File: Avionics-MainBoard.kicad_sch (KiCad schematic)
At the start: 4 parts

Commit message: v3 Layout complete
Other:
- sheet Connectors ports: added COIL_EN, HEATER0_ON, HEATER1_ON, HEATER_ENABLE, RW_EN; removed none
- sheet LoRa ports: added LoRa_CSn, LoRa_FLT; removed CSn
- sheet MCU_IO ports: added 3V3_M_RST, 3V3_P_EN, 3V3_P_FLT, COIL_EN, GPS_EN, GPS_FLT, HEATER0_ON, HEATER1_ON, HEATER_ENABLE, LoRa_FLT, Payload_CSn, Payload_EN, Payload_FLT, Payload_IO0, Payload_IO1, Payload_IO2, RW_EN; removed 3V3_RST
- sheet Main Power ports: added 3V3_P_FLT; removed none
- sheet Payload ports: added CLK, MISO, MOSI, Payload_CSn, Payload_EN, Payload_FLT, Payload_IO0, Payload_IO1, Payload_IO2; removed none
- sheet SD ports: added SD_CSn; removed CSn

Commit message: v4.0 Updates
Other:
- removed sheet Payload
- sheet Connectors ports: added RW_MOTOR_ALRM, RW_MOTOR_FLT, RW_POWER_FLT; removed none
- sheet MCU_IO ports: added none; removed Payload_CSn, Payload_EN, Payload_FLT, Payload_IO0, Payload_IO1, Payload_IO2
- note added: "TODO: CLEANUP"
- note added: "Unconnected Cutting RW from Argus 1/2"
- moved on the sheet: H1, H2, H3, H4

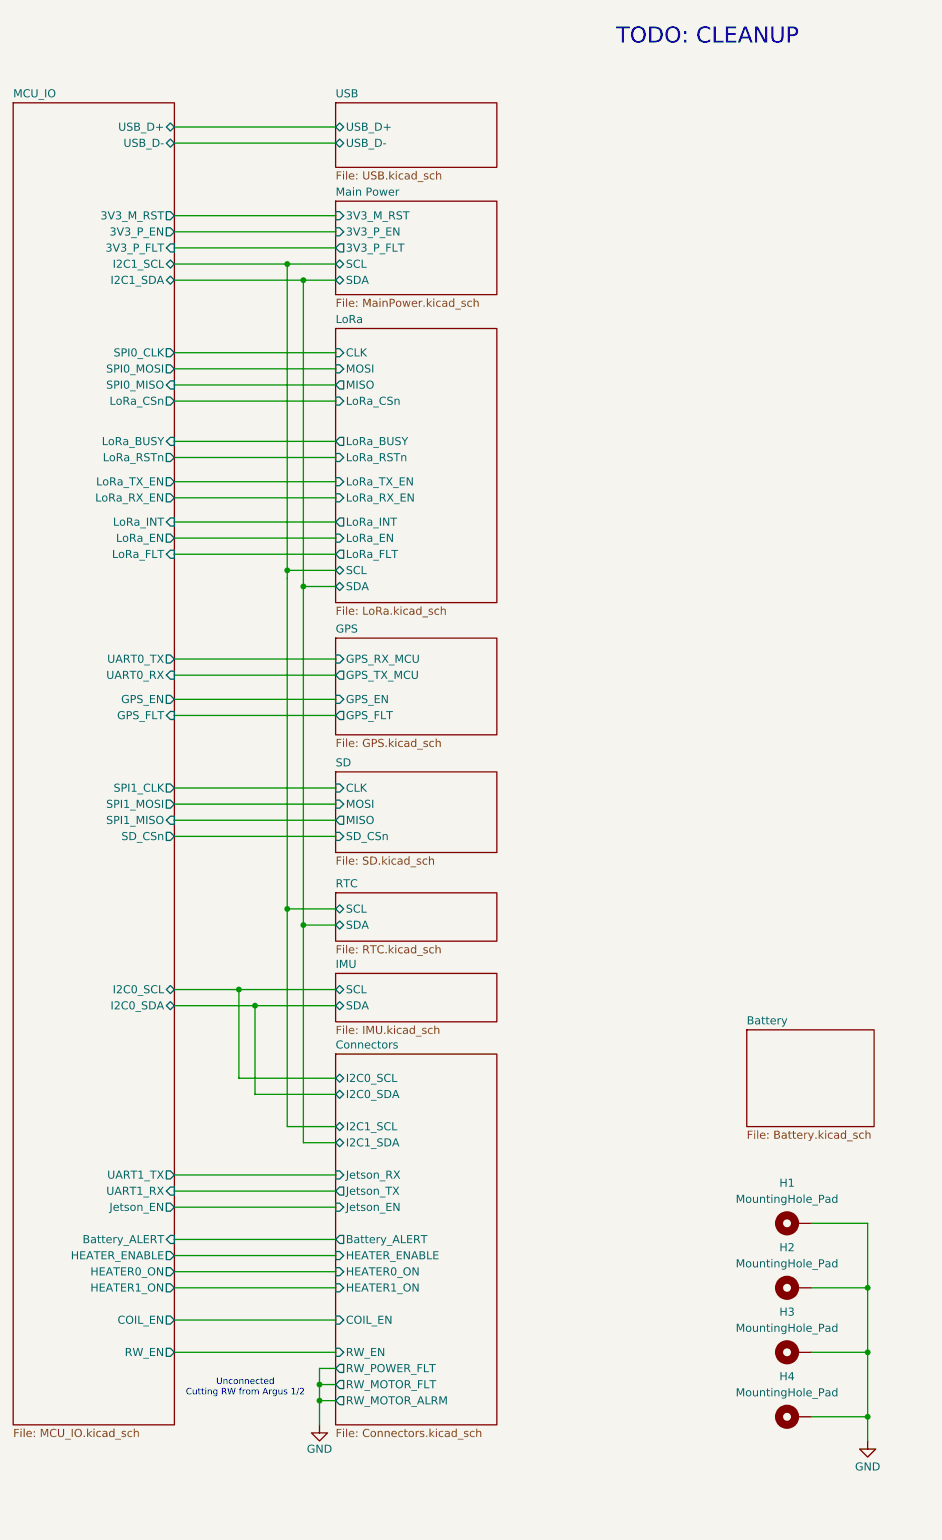
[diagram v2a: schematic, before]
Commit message: Fixed Jetson FPC pinout
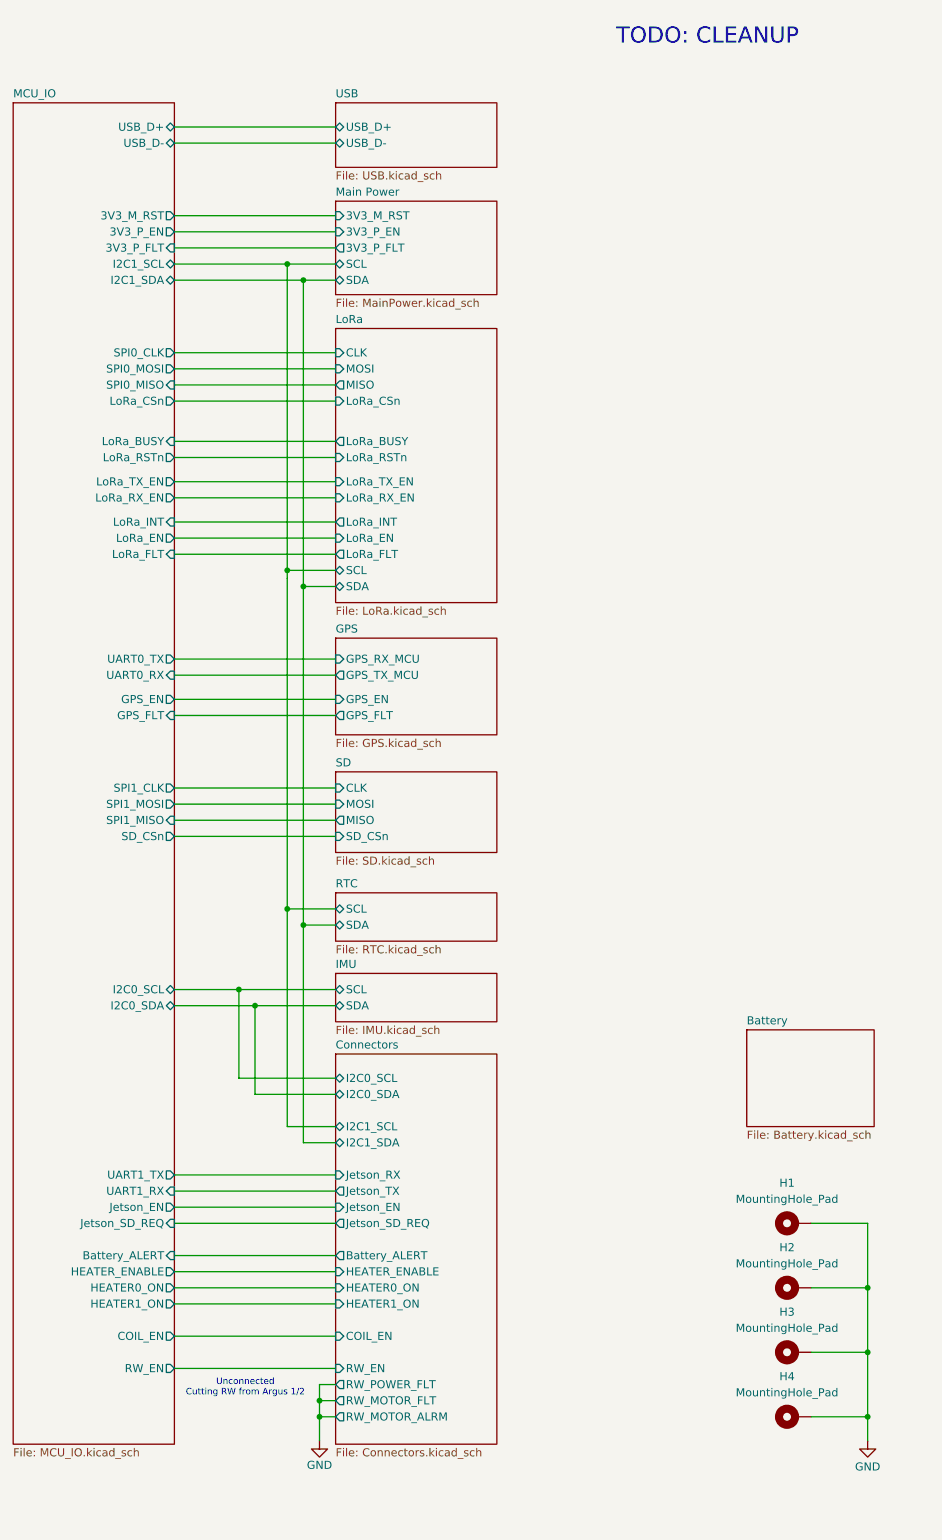
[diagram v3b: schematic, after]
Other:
- sheet Connectors ports: added Jetson_SD_REQ; removed none
- sheet MCU_IO ports: added Jetson_SD_REQ; removed none
